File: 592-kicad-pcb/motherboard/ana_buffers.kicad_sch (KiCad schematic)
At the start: 7 parts, among them J1 U.FL, J2 U.FL, U1 OPA2328DGKR, U2 74LVC1T45GW

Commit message: updates to routing
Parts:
- renumbered U1 to U2, U2 to U3
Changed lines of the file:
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@@
 		(dnp no)
 		(fields_autoplaced yes)
-		(property "Reference" "#PWR05"
+		(property "Reference" "#PWR06"
 			(at 97.79 102.87 0)
 			(effects
@@
 			(project "motherboard"
 				(path "/5b0c97ac-fa03-4db8-b41b-0eee32b6f55d/f049e4ad-bebe-4338-850a-2727de737ae9/cc4799d4-5517-451a-9b97-5b1497b0c7e9"
-					(reference "#PWR05")
+					(reference "#PWR06")
 					(unit 1)
 				)
@@
 		(dnp no)
 		(fields_autoplaced yes)
-		(property "Reference" "#PWR02"
+		(property "Reference" "#PWR03"
 			(at 59.69 63.5 0)
 			(effects
@@
 			(project "motherboard"
 				(path "/5b0c97ac-fa03-4db8-b41b-0eee32b6f55d/f049e4ad-bebe-4338-850a-2727de737ae9/cc4799d4-5517-451a-9b97-5b1497b0c7e9"
-					(reference "#PWR02")
+					(reference "#PWR03")
 					(unit 1)
 				)
@@
 		(dnp no)
 		(fields_autoplaced yes)
-		(property "Reference" "#PWR07"
+		(property "Reference" "#PWR08"
 			(at 152.4 88.9 0)
 			(effects
@@
 			(project "motherboard"
 				(path "/5b0c97ac-fa03-4db8-b41b-0eee32b6f55d/f049e4ad-bebe-4338-850a-2727de737ae9/cc4799d4-5517-451a-9b97-5b1497b0c7e9"
-					(reference "#PWR07")
+					(reference "#PWR08")
 					(unit 1)
 				)
@@
 		(dnp no)
 		(fields_autoplaced yes)
-		(property "Reference" "#PWR03"
+		(property "Reference" "#PWR04"
 			(at 59.69 121.92 0)
 			(effects
@@
 			(project "motherboard"
 				(path "/5b0c97ac-fa03-4db8-b41b-0eee32b6f55d/f049e4ad-bebe-4338-850a-2727de737ae9/cc4799d4-5517-451a-9b97-5b1497b0c7e9"
-					(reference "#PWR03")
+					(reference "#PWR04")
 					(unit 1)
 				)
@@
 		(on_board yes)
 		(dnp no)
-		(property "Reference" "U2"
+		(property "Reference" "U3"
 			(at 152.146 59.944 0)
 			(effects
@@
 			(project "motherboard"
 				(path "/5b0c97ac-fa03-4db8-b41b-0eee32b6f55d/f049e4ad-bebe-4338-850a-2727de737ae9/cc4799d4-5517-451a-9b97-5b1497b0c7e9"
-					(reference "U2")
+					(reference "U3")
 					(unit 1)
 				)
@@
 		(dnp no)
 		(fields_autoplaced yes)
-		(property "Reference" "#PWR08"
+		(property "Reference" "#PWR09"
 			(at 165.1 68.58 0)
 			(effects
@@
 			(project "motherboard"
 				(path "/5b0c97ac-fa03-4db8-b41b-0eee32b6f55d/f049e4ad-bebe-4338-850a-2727de737ae9/cc4799d4-5517-451a-9b97-5b1497b0c7e9"
-					(reference "#PWR08")
+					(reference "#PWR09")
 					(unit 1)
 				)
@@
 		(dnp no)
 		(fields_autoplaced yes)
-		(property "Reference" "#PWR04"
+		(property "Reference" "#PWR05"
 			(at 97.79 86.36 0)
 			(effects
@@
 			(project "motherboard"
 				(path "/5b0c97ac-fa03-4db8-b41b-0eee32b6f55d/f049e4ad-bebe-4338-850a-2727de737ae9/cc4799d4-5517-451a-9b97-5b1497b0c7e9"
-					(reference "#PWR04")
+					(reference "#PWR05")
 					(unit 1)
 				)
@@
 		(on_board yes)
 		(dnp no)
-		(property "Reference" "U1"
+		(property "Reference" "U2"
 			(at 61.8333 73.66 0)
 			(effects
@@
 			(project "motherboard"
 				(path "/5b0c97ac-fa03-4db8-b41b-0eee32b6f55d/f049e4ad-bebe-4338-850a-2727de737ae9/cc4799d4-5517-451a-9b97-5b1497b0c7e9"
-					(reference "U1")
+					(reference "U2")
 					(unit 1)
 				)
@@
 		(dnp no)
 		(fields_autoplaced yes)
-		(property "Reference" "#PWR01"
+		(property "Reference" "#PWR02"
 			(at 54.61 77.47 0)
 			(effects
@@
 			(project "motherboard"
 				(path "/5b0c97ac-fa03-4db8-b41b-0eee32b6f55d/f049e4ad-bebe-4338-850a-2727de737ae9/cc4799d4-5517-451a-9b97-5b1497b0c7e9"
-					(reference "#PWR01")
+					(reference "#PWR02")
 					(unit 1)
 				)
@@
 		(dnp no)
 		(fields_autoplaced yes)
-		(property "Reference" "#PWR06"
+		(property "Reference" "#PWR07"
 			(at 139.7 68.58 0)
 			(effects
@@
 			(project "motherboard"
 				(path "/5b0c97ac-fa03-4db8-b41b-0eee32b6f55d/f049e4ad-bebe-4338-850a-2727de737ae9/cc4799d4-5517-451a-9b97-5b1497b0c7e9"
-					(reference "#PWR06")
+					(reference "#PWR07")
 					(unit 1)
 				)

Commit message: finalize termination
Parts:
- added R78, R79, R80: 100, Resistor_SMD:R_0402_1005Metric, symbol Device:R_Small
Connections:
- net ANA_MUX_OUT_1_BUF: now also R78.1; no longer U2.1 (Vout1)
- net ANA_MUX_OUT_2_BUF: now also R79.1; no longer U2.7 (Vout2)
- net NFC_AFE_TDO_EXT_BUF: now also R80.1; no longer U3.3 (A)
- new net: R78.2, U2.1 (Vout1)
- new net: R80.2, U3.3 (A)
- new net: R79.2, U2.7 (Vout2)
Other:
- moved on the sheet: J1, J2

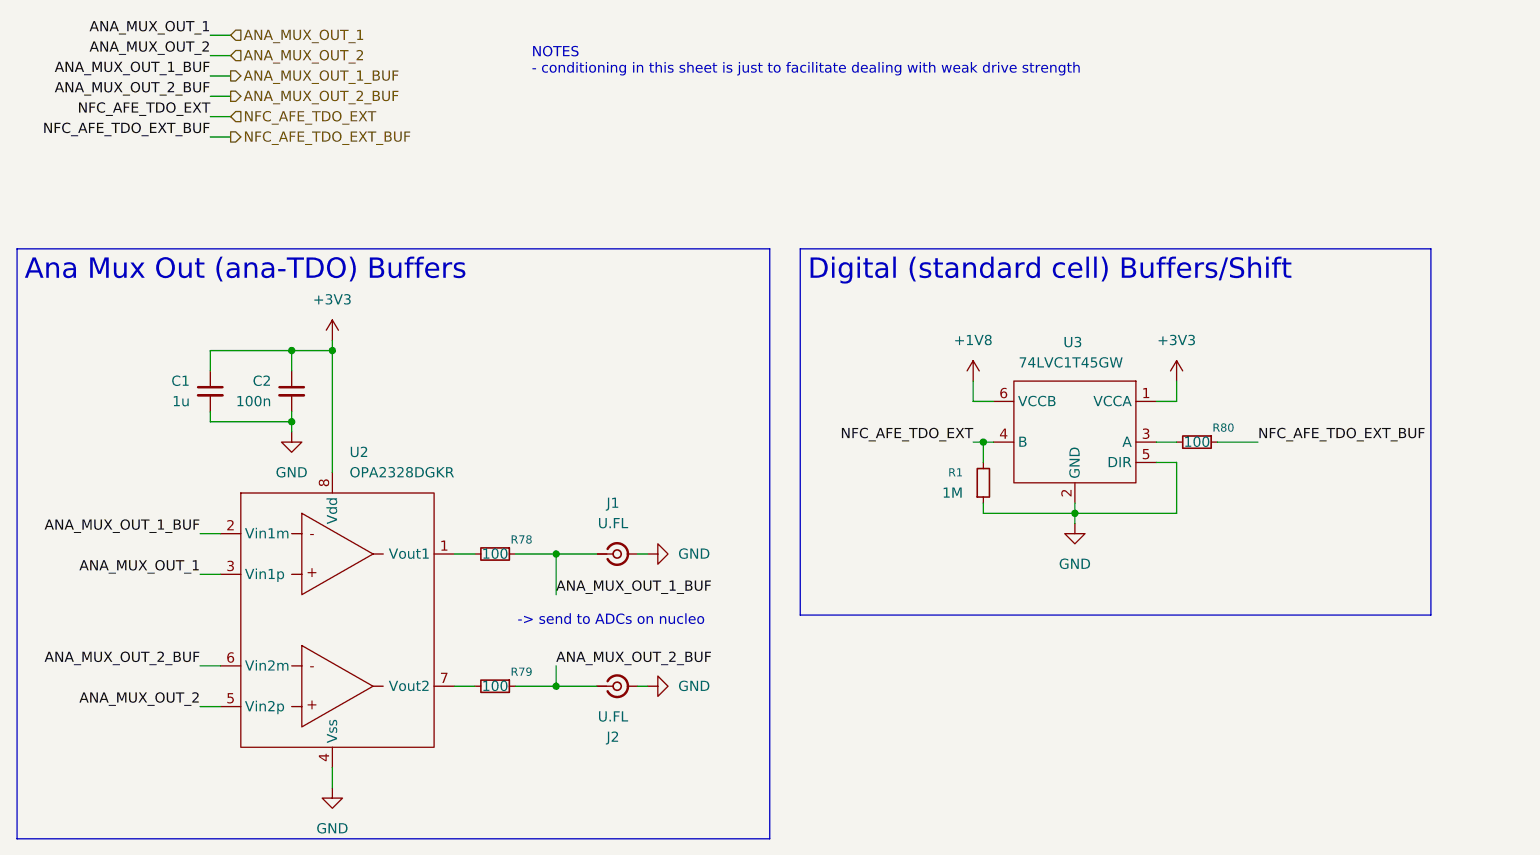
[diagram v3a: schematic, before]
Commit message: core routing progress
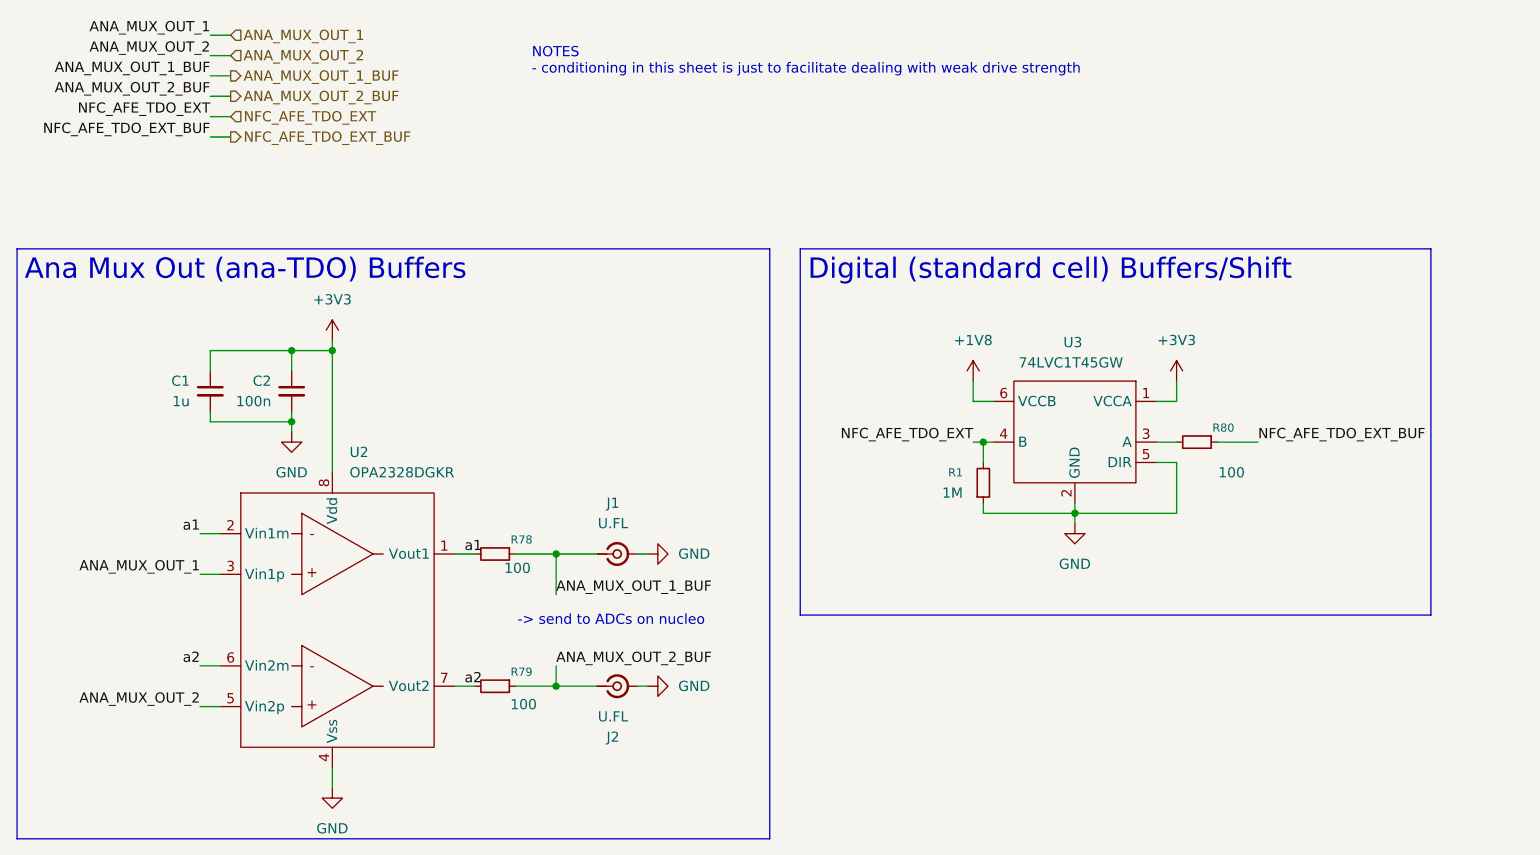
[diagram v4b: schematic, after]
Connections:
- net ANA_MUX_OUT_1_BUF: no longer U2.2 (Vin1m)
- net ANA_MUX_OUT_2_BUF: no longer U2.6 (Vin2m)
- net a1: now reaches R78.2, U2.1 (Vout1)
- net a1: now also U2.2 (Vin1m)
- net a2: now reaches R79.2, U2.7 (Vout2)
- net a2: now also U2.6 (Vin2m)
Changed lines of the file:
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@@
+		)
+	)
+	(label "a2"
+		(at 43.18 100.33 180)
+		(effects
+			(font
+				(size 1.27 1.27)
+			)
+			(justify right bottom)
+		)
+	)
+	(label "a1"
+		(at 43.18 83.82 180)
+		(effects
+			(font
+				(size 1.27 1.27)
+			)
+			(justify right bottom)
+		)
+	)
+	(label "a1"
+		(at 76.2 86.36 0)
+		(effects
+			(font
+				(size 1.27 1.27)
+			)
+			(justify left bottom)
+		)
+	)
+	(label "a2"
+		(at 76.2 102.87 0)
+		(effects
+			(font
+				(size 1.27 1.27)
+			)
+			(justify left bottom)
 		)
 	)
@@
 	(label "ANA_MUX_OUT_2"
 		(at 44.45 24.13 180)
-		(effects
-			(font
-				(size 1.27 1.27)
-			)
-			(justify right bottom)
-		)
-	)
-	(label "ANA_MUX_OUT_2_BUF"
-		(at 43.18 100.33 180)
-		(effects
-			(font
-				(size 1.27 1.27)
-			)
-			(justify right bottom)
-		)
-	)
-	(label "ANA_MUX_OUT_1_BUF"
-		(at 43.18 83.82 180)
 		(effects
 			(font
@@
 		)
 		(property "Value" "100"
-			(at 80.01 86.36 90)
+			(at 82.804 88.138 90)
 			(effects
 				(font
@@
 		)
 		(property "Value" "100"
-			(at 80.01 102.87 90)
+			(at 83.566 105.156 90)
 			(effects
 				(font
@@
 		)
 		(property "Value" "100"
-			(at 167.64 72.39 90)
-			(effects
-				(font
+			(at 171.958 76.2 90)
+			(effects
+				(font
